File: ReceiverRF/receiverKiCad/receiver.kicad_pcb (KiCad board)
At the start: 2 copper layers, 95.4 x 60 mm, 69 parts, among them J1 Conn_Coaxial, J2 Conn_01x05_Socket, J3 Conn_01x04, Q1 MMBT3904, SW1 SW_Push, SW2 SW_Push, SW3 SW_Push, SW4 SW_Push, SW5 SW_SPST, U1 STM32F103RET6, U2 NCV5501DT33RKG, U3 NJM2882F05-TE1, U4 MLX90393SLW-ABA-011-RE, Y1 Crystal_GND24

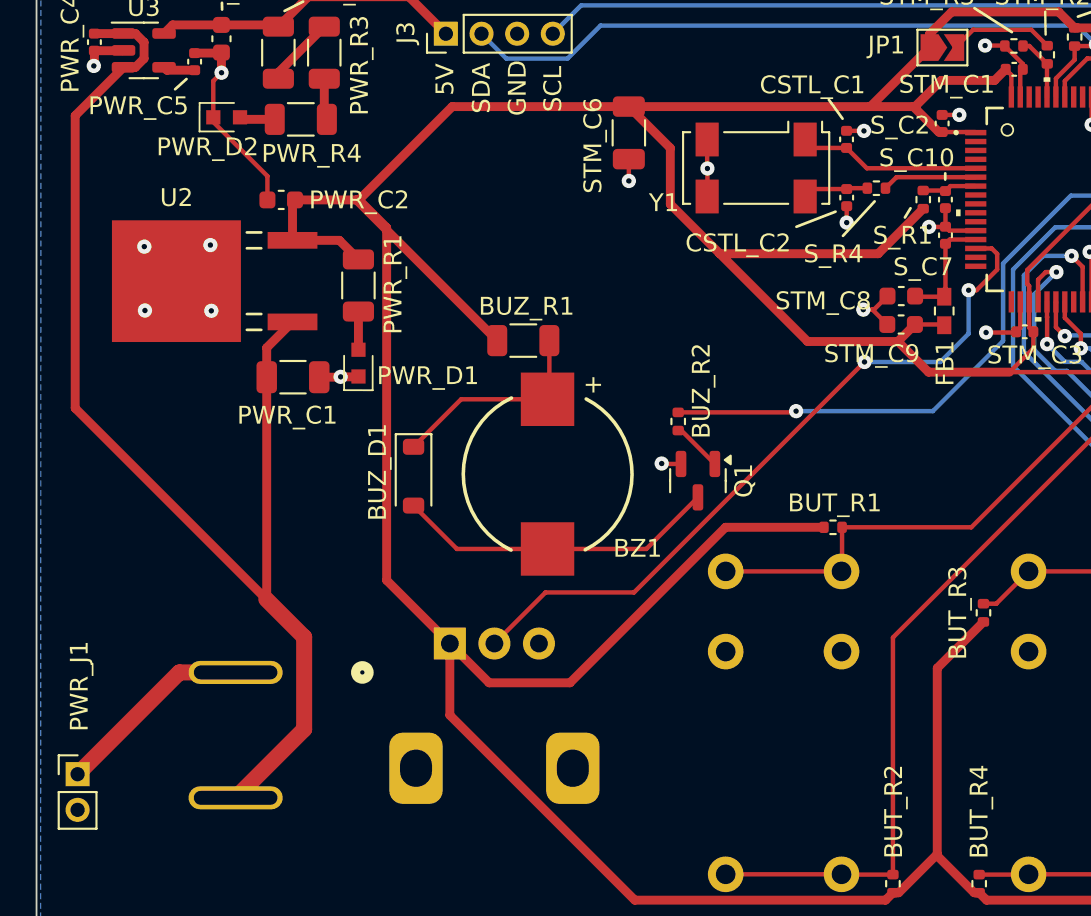
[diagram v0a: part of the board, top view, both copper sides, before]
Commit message: changement switch pour switch plus petite
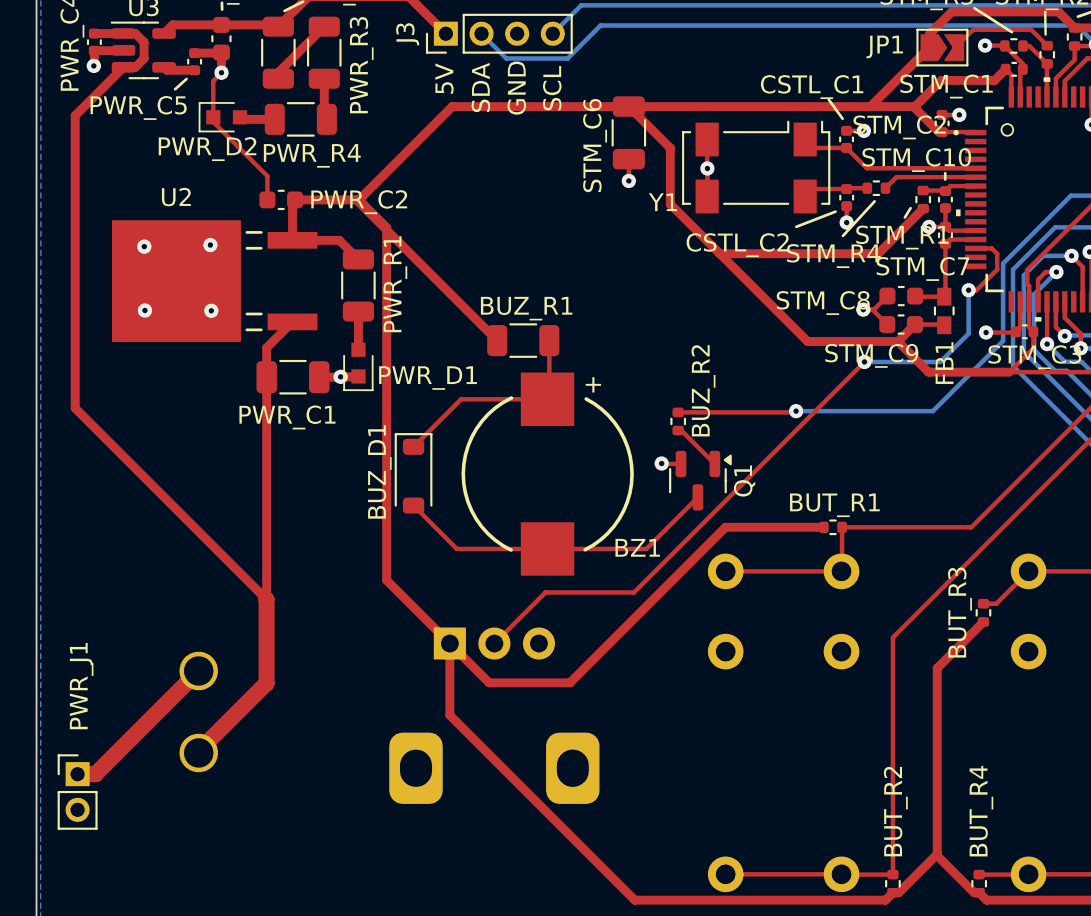
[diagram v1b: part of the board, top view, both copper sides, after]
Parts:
- SW5: footprint Footprints:D102J12S215PQA_CNK -> Footprints:SW_1MS02Q_CNK
- moved SW5 2.07 mm to (108.9, 119.2)
- renumbered S_C10 to STM_C10, S_C2 to STM_C2, S_C7 to STM_C7, S_R1 to STM_R1, S_R4 to STM_R4
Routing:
- net VCC: track 70.5 -> 67.1 mm
- net Net-(PWR_J1-Pin_1): track 11.2 -> 9.20 mm
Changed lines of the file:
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@@
 		(descr "Resistor SMD 0402 (1005 Metric), square (rectangular) end terminal, IPC_7351 nominal, (Body size source: IPC-SM-782 page 72, https://www.pcb-3d.com/wordpress/wp-content/uploads/ipc-sm-782a_amendment_1_and_2.pdf), generated with kicad-footprint-generator")
 		(tags "resistor")
-		(property "Reference" "S_R1"
+		(property "Reference" "STM_R1"
 			(at -2.013176 -1.146563 180)
 			(layer "F.SilkS")
@@
 		(descr "Resistor SMD 0402 (1005 Metric), square (rectangular) end terminal, IPC_7351 nominal, (Body size source: IPC-SM-782 page 72, https://www.pcb-3d.com/wordpress/wp-content/uploads/ipc-sm-782a_amendment_1_and_2.pdf), generated with kicad-footprint-generator")
 		(tags "resistor")
-		(property "Reference" "S_R4"
+		(property "Reference" "STM_R4"
 			(at -2.40438 3.693556 180)
 			(layer "F.SilkS")
@@
 		(descr "Capacitor SMD 0402 (1005 Metric), square (rectangular) end terminal, IPC_7351 nominal, (Body size source: IPC-SM-782 page 76, https://www.pcb-3d.com/wordpress/wp-content/uploads/ipc-sm-782a_amendment_1_and_2.pdf), generated with kicad-footprint-generator")
 		(tags "capacitor")
-		(property "Reference" "S_C10"
+		(property "Reference" "STM_C10"
 			(at -2.336032 1.608575 180)
 			(layer "F.SilkS")
@@
 		(descr "Capacitor SMD 0402 (1005 Metric), square (rectangular) end terminal, IPC_7351 nominal, (Body size source: IPC-SM-782 page 76, https://www.pcb-3d.com/wordpress/wp-content/uploads/ipc-sm-782a_amendment_1_and_2.pdf), generated with kicad-footprint-generator")
 		(tags "capacitor")
-		(property "Reference" "S_C7"
+		(property "Reference" "STM_C7"
 			(at -1.776391 -1.246615 180)
 			(layer "F.SilkS")
@@
 		(descr "Capacitor SMD 0402 (1005 Metric), square (rectangular) end terminal, IPC_7351 nominal, (Body size source: IPC-SM-782 page 76, https://www.pcb-3d.com/wordpress/wp-content/uploads/ipc-sm-782a_amendment_1_and_2.pdf), generated with kicad-footprint-generator")
 		(tags "capacitor")
-		(property "Reference" "S_C2"
+		(property "Reference" "STM_C2"
 			(at -0.104887 -2.36386 0)
 			(layer "F.SilkS")
@@
 		(tags "Potentiometer vertical Alps RK09K RK09D Single Snapin")
 		(property "Reference" "RV1"
-			(at 14.582282 -2.985096 360)
+			(at 14.582282 -2.985096 0)
 			(layer "B.SilkS")
 			(effects
@@
 		)
 	)
-	(footprint "Footprints:D102J12S215PQA_CNK"
+	(footprint "Footprints:SW_1MS02Q_CNK"
 		(layer "B.Cu")
-		(at 110.993874 119.288911 180)
-		(tags "D102J12S215PQA ")
+		(at 108.922352 119.208122 180)
+		(tags "L101011MS02Q ")
 		(property "Reference" "SW5"
-			(at -0.112105 4.653657 0)
+			(at -2.855001 -4.600001 0)
 			(unlocked yes)
 			(layer "B.SilkS")
+			(hide yes)
 			(effects
 				(font
 					(size 1 1)
-					(thickness 0.153)
+					(thickness 0.15)
 				)
 				(justify mirror)
@@
 		)
 		(property "Value" "SW_SPST"
-			(at 0 -7.0358 0)
+			(at -2.855001 -4.600001 0)
 			(unlocked yes)
 			(layer "B.Fab")
@@
 			)
 		)
-		(property "Footprint" "Footprints:D102J12S215PQA_CNK"
+		(property "Footprint" "Footprints:SW_1MS02Q_CNK"
 			(at 0 0 0)
 			(layer "B.Fab")
@@
 			)
 		)
-		(property "Datasheet" "https://www.digikey.ca/en/products/detail/c-k/D102J12S215PQA/768267"
+		(property "Datasheet" "https://www.digikey.ca/en/products/detail/c-k/L101011MS02Q/484142"
 			(at 0 0 0)
 			(layer "B.Fab")
@@
 		(attr through_hole)
 		(fp_line
-			(start 6.477 3.5052)
-			(end 6.477 -17.5768)
+			(start 2.669499 5.077399)
+			(end 2.669499 -14.277401)
 			(stroke
 				(width 0.1524)
@@
 		)
 		(fp_line
-			(start 6.477 -17.5768)
-			(end -6.477 -17.5768)
+			(start 2.669499 -14.277401)
+			(end -8.379501 -14.277401)
 			(stroke
 				(width 0.1524)
@@
 		)
 		(fp_line
-			(start -6.477 3.5052)
-			(end 6.477 3.5052)
+			(start -8.379501 5.077399)
+			(end 2.669499 5.077399)
 			(stroke
 				(width 0.1524)
@@
 		)
 		(fp_line
-			(start -6.477 -17.5768)
-			(end -6.477 3.5052)
+			(start -8.379501 -14.277401)
+			(end -8.379501 5.077399)
 			(stroke
 				(width 0.1524)
@@
 			(layer "B.SilkS")
 		)
-		(fp_circle
-			(center -7.112 0)
-			(end -6.731 0)
+		(fp_line
+			(start 2.796499 5.204399)
+			(end 2.796499 -14.404401)
 			(stroke
-				(width 0.508)
+				(width 0.1524)
 				(type solid)
 			)
-			(fill none)
-			(layer "B.SilkS")
+			(layer "B.CrtYd")
 		)
-		(fp_circle
-			(center -7.112 0)
-			(end -6.731 0)
+		(fp_line
+			(start 2.796499 -14.404401)
+			(end -8.506501 -14.404401)
 			(stroke
-				(width 0.508)
+				(width 0.1524)
 				(type solid)
 			)
-			(fill none)
-			(layer "F.SilkS")
+			(layer "B.CrtYd")
 		)
 		(fp_line
-			(start 6.604 3.6322)
-			(end 6.604 -17.7038)
+			(start -8.506501 5.204399)
+			(end 2.796499 5.204399)
 			(stroke
 				(width 0.1524)
@@
 		)
 		(fp_line
-			(start 6.604 -17.7038)
-			(end -6.604 -17.7038)
+			(start -8.506501 -14.404401)
+			(end -8.506501 5.204399)
 			(stroke
 				(width 0.1524)
@@
 		)
 		(fp_line
-			(start -6.604 3.6322)
-			(end 6.604 3.6322)
+			(start 2.542499 4.950399)
+			(end 2.542499 -14.150401)
 			(stroke
-				(width 0.1524)
+				(width 0.0254)
 				(type solid)
 			)
-			(layer "B.CrtYd")
+			(layer "B.Fab")
 		)
 		(fp_line
-			(start -6.604 -17.7038)
-			(end -6.604 3.6322)
+			(start 2.542499 -14.150401)
+			(end -8.252501 -14.150401)
 			(stroke
-				(width 0.1524)
+				(width 0.0254)
 				(type solid)
 			)
-			(layer "B.CrtYd")
+			(layer "B.Fab")
 		)
 		(fp_line
-			(start 6.35 3.3782)
-			(end 6.35 -17.4498)
+			(start -1.267501 -2.060001)
+			(end -4.442501 -2.060001)
 			(stroke
 				(width 0.0254)
@@
 		)
 		(fp_line
-			(start 6.35 -17.4498)
-			(end -6.35 -17.4498)
+			(start -1.267501 -7.140001)
+			(end -1.267501 -2.060001)
 			(stroke
 				(width 0.0254)
@@
 		)
 		(fp_line
-			(start -6.35 3.3782)
-			(end 6.35 3.3782)
+			(start -4.442501 -2.060001)
+			(end -4.442501 -7.140001)
 			(stroke
 				(width 0.0254)
@@
 		)
 		(fp_line
-			(start -6.35 -17.4498)
-			(end -6.35 3.3782)
+			(start -4.442501 -7.140001)
+			(end -1.267501 -7.140001)
 			(stroke
 				(width 0.0254)
@@
 			(layer "B.Fab")
 		)
+		(fp_line
+			(start -8.252501 4.950399)
+			(end 2.542499 4.950399)
+			(stroke
+				(width 0.0254)
+				(type solid)
+			)
+			(layer "B.Fab")
+		)
+		(fp_line
+			(start -8.252501 -14.150401)
+			(end -8.252501 4.950399)
+			(stroke
+				(width 0.0254)
+				(type solid)
+			)
+			(layer "B.Fab")
+		)
+		(fp_poly
+			(pts
+				(xy -4.442501 -7.140001) (xy -4.442501 -4.600001) (xy -1.267501 -4.600001) (xy -1.267501 -7.140001)
+			)
+			(stroke
+				(width 0)
+				(type solid)
+			)
+			(fill solid)
+			(layer "B.Fab")
+		)
+		(fp_text user "*"
+			(at 1.909999 7.62 0)
+			(unlocked yes)
+			(layer "B.Fab")
+			(effects
+				(font
+					(size 1 1)
+					(thickness 0.15)
+				)
+				(justify mirror)
+			)
+		)
+		(fp_text user "*"
+			(at 1.909999 7.62 0)
+			(unlocked yes)
+			(layer "B.Fab")
+			(effects
+				(font
+					(size 1 1)
+					(thickness 0.15)
+				)
+				(justify mirror)
+			)
+		)
 		(fp_text user "${REFERENCE}"
-			(at 0 -7.0358 0)
+			(at -2.855001 -4.600001 0)
 			(unlocked yes)
 			(layer "B.Fab")
@@
 			)
 		)
-		(pad "1" thru_hole oval
+		(pad "1" thru_hole circle
 			(at 0 0 180)
-			(size 5.2878 1.2954)
-			(drill oval 4.7 0.7874)
+			(size 2.159 2.159)
+			(drill 1.651)
 			(layers "*.Cu" "*.Mask")
 			(remove_unused_layers no)
@@
 			(pintype "passive")
 		)
-		(pad "2" thru_hole oval
-			(at 0 -7.0358 180)
-			(size 5.2878 1.2954)
-			(drill oval 4.7 0.7874)
+		(pad "2" thru_hole circle
+			(at 0 -4.600001 180)
+			(size 2.159 2.159)
+			(drill 1.651)
 			(layers "*.Cu" "*.Mask")
 			(remove_unused_layers no)
@@
 			(pintype "passive")
 		)
-		(model "${KIPRJMOD}/librairie-receiver/lib_3D/D102J12S215PQA.stp"
+		(model "${KIPRJMOD}/librairie-receiver/lib_3D/L101011MS02Q.stp"
 			(offset
-				(xyz 0 -7 13)
+				(xyz -3 -4.5 1.5)
 			)
 			(scale
@@
 	)
 	(segment
-		(start 114.840203 122.478382)
-		(end 114.840203 117.307027)
-		(width 0.9)
-		(layer "F.Cu")
-		(net 30)
-	)
-	(segment
 		(start 101.989795 88.041697)
 		(end 104.70212 85.329372)
@@
 	)
 	(segment
+		(start 112.728657 119.89637)
+		(end 108.922352 123.702675)
+		(width 0.9)
+		(layer "F.Cu")
+		(net 30)
+	)
+	(segment
 		(start 112.738326 102.720151)
 		(end 112.738326 101.067823)
@@
 	)
 	(segment
+		(start 112.728657 115.195482)
+		(end 112.728657 119.89637)
+		(width 0.9)
+		(layer "F.Cu")
+		(net 30)
+	)
+	(segment
 		(start 112.738326 115.152419)
 		(end 112.71196 115.178785)
@@
 	)
 	(segment
-		(start 114.840203 117.307027)
-		(end 112.71196 115.178785)
-		(width 0.9)
-		(layer "F.Cu")
-		(net 30)
-	)
-	(segment
 		(start 105.855285 84.838706)
 		(end 105.855285 83.920038)
@@
 	)
 	(segment
-		(start 112.71196 115.178785)
-		(end 101.989795 104.456619)
-		(width 0.5)
+		(start 108.922352 123.702675)
+		(end 108.922352 123.808123)
+		(width 0.9)
 		(layer "F.Cu")
 		(net 30)
 	)
 	(segment
-		(start 110.993874 126.324711)
-		(end 114.840203 122.478382)
-		(width 0.9)
+		(start 112.71196 115.178785)
+		(end 101.989795 104.456619)
+		(width 0.5)
 		(layer "F.Cu")
 		(net 30)
@@
 	)
 	(segment
+		(start 112.71196 115.178785)
+		(end 112.728657 115.195482)
+		(width 0.9)
+		(layer "F.Cu")
+		(net 30)
+	)
+	(segment
 		(start 105.364619 83.429372)
 		(end 104.70212 83.429372)
@@
 	)
 	(segment
-		(start 107.836493 119.288911)
-		(end 102.1247 125.000704)
+		(start 108.922352 119.208122)
+		(end 103.12977 125.000704)
 		(width 0.9)
 		(layer "F.Cu")
@@
 	)
 	(segment
-		(start 110.993874 119.288911)
-		(end 107.836493 119.288911)
+		(start 103.12977 125.000704)
+		(end 102.1247 125.000704)
 		(width 0.9)
 		(layer "F.Cu")

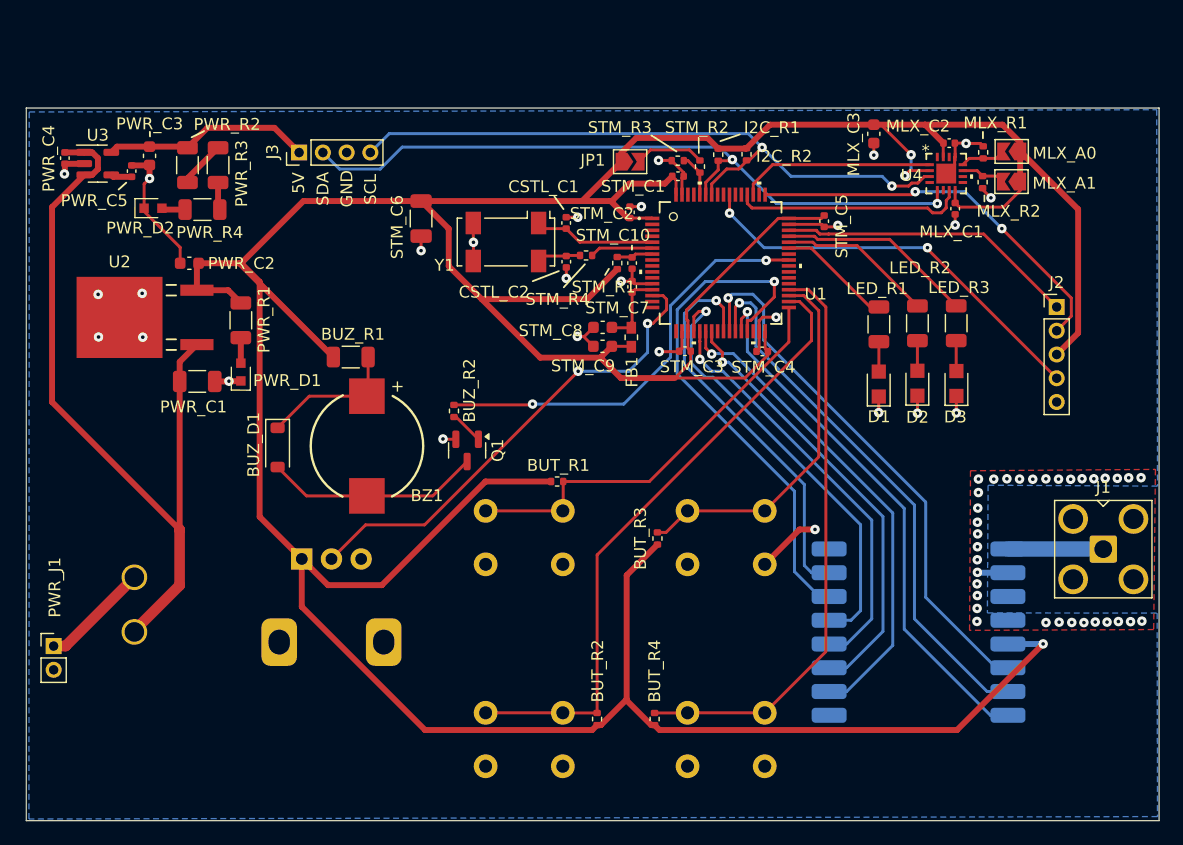
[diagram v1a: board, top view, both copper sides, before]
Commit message: mounting holes et Logo
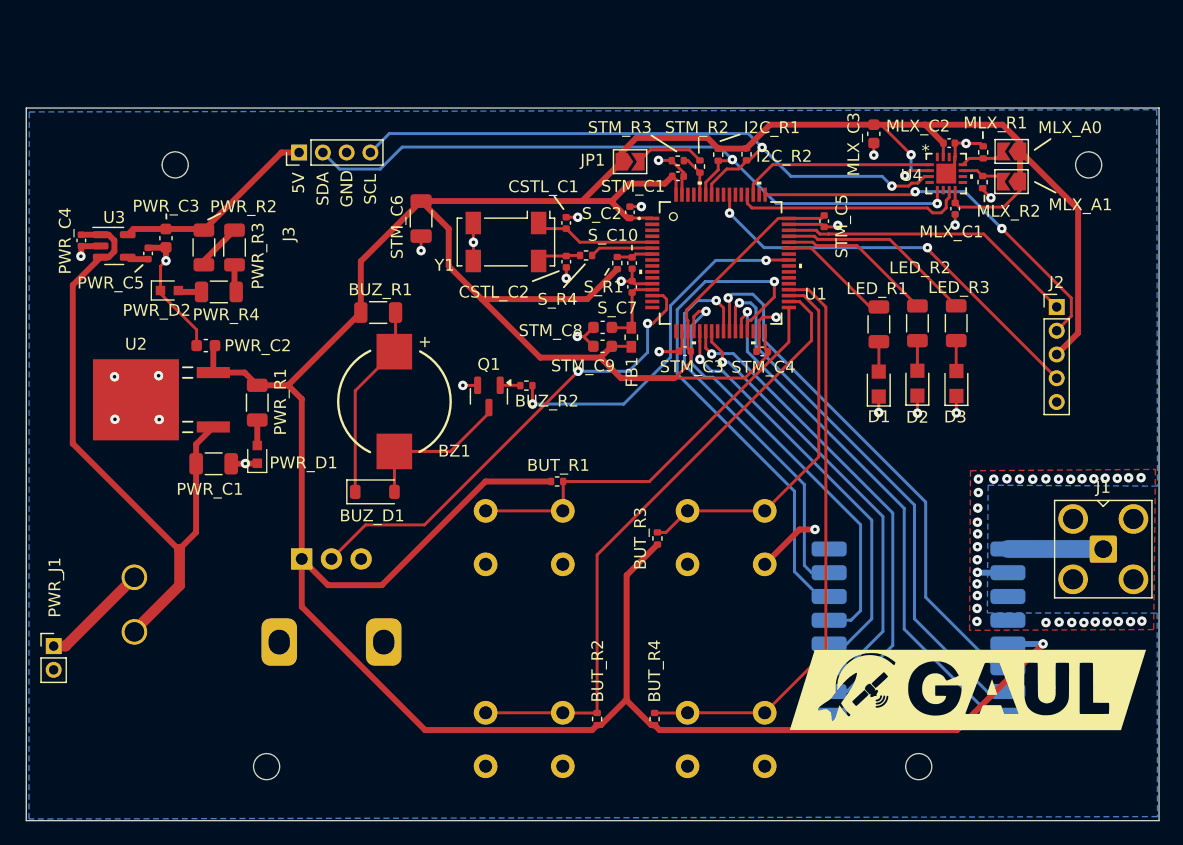
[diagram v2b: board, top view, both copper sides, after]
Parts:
- added G***: LOGO, Footprints:logo, F.Cu at (179.1, 128.7)
- added REF**: MountingHole_2.2mm_M2, MountingHole:MountingHole_2.2mm_M2, F.Cu at (120.1, 135.2)
- added REF**: MountingHole_2.2mm_M2, MountingHole:MountingHole_2.2mm_M2, F.Cu at (175.0, 135.2)
- added REF**: MountingHole_2.2mm_M2, MountingHole:MountingHole_2.2mm_M2, F.Cu at (189.3, 84.5)
- added REF**: MountingHole_2.2mm_M2, MountingHole:MountingHole_2.2mm_M2, F.Cu at (112.4, 84.5)
- moved BUZ_D1 9.00 mm to (129.2, 112.0), turned to 0 degrees
- moved PWR_C2 7.07 mm to (114.9, 99.7)
- moved PWR_C3 7.07 mm to (111.6, 90.7)
- moved PWR_C4 7.07 mm to (104.5, 90.8)
- moved PWR_D1 7.07 mm to (119.3, 108.9)
- moved PWR_C1 7.07 mm to (115.6, 109.7)
- moved PWR_C5 7.07 mm to (110.1, 91.9)
- moved PWR_D2 7.07 mm to (111.9, 95.1)
- moved PWR_R1 7.07 mm to (119.3, 104.5)
- moved PWR_R2 7.07 mm to (114.8, 91.4)
- moved PWR_R3 7.07 mm to (117.4, 91.4)
- moved PWR_R4 7.07 mm to (116.0, 95.2)
- moved U2 7.07 mm to (109.1, 104.3)
- moved U3 7.07 mm to (107.2, 91.3)
- moved BUZ_R2 6.46 mm to (141.9, 103.1), turned to 180 degrees
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- renumbered STM_C10 to S_C10, STM_C2 to S_C2, STM_C7 to S_C7, STM_R1 to S_R1, STM_R4 to S_R4
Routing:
- net +3.3V: track 373.2 -> 351.9 mm
- net VCC: track 67.1 -> 54.6 mm
- net Net-(BUZ_D1-A): track 18.2 -> 13.2 mm
- net BUZZER: track 35.8 -> 30.8 mm
- net Net-(BUZ_D1-K): track 12.0 -> 16.5 mm
- net Net-(Q1-B): track 2.83 -> 1.71 mm
